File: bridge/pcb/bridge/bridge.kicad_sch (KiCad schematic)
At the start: 14 parts, among them J1 Screw_Terminal_01x06, J2 Screw_Terminal_01x06, J3 Screw_Terminal_01x06, J4 Conn_01x23, SW1 SW_SPST, U2 J104D2C12VDC.20S

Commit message: Completed schematic
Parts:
- added R11: 47k, bridge:THT_RESISTOR_WITH_VALUE, symbol Device:R
- added R12: 100k, bridge:THT_RESISTOR_WITH_VALUE, symbol Device:R
- R6, R7, R8, R9: footprint Resistor_THT:R_Axial_DIN0309_L9.0mm_D3.2mm_P12.70mm_Horizontal -> bridge:THT_RESISTOR_WITH_VALUE
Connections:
- net GND: now also R11.1
- net at R6.1, SW1.1 (A), U2.8: now also R12.2
- new net MAN_AUTO_STATE: R11.2, R12.1
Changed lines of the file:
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@@
     (company "Roman Rice")
   )
+  (junction (at 110.49 144.78) (diameter 0) (color 0 0 0 0)
+  )
   (junction (at 226.06 106.68) (diameter 0) (color 0 0 0 0)
   )
+  (junction (at 110.49 166.37) (diameter 0) (color 0 0 0 0)
+  )
   (junction (at 95.25 144.78) (diameter 0) (color 0 0 0 0)
   )
   (junction (at 111.76 43.18) (diameter 0) (color 0 0 0 0)
+  )
+  (junction (at 128.27 144.78) (diameter 0) (color 0 0 0 0)
   )
   (no_connect (at 228.6 111.76))
@@
     (stroke (width 0) (type default))
   )
+  (wire (pts (xy 128.27 153.67) (xy 128.27 166.37))
+    (stroke (width 0) (type default))
+  )
   (wire (pts (xy 60.96 76.2) (xy 41.91 76.2))
     (stroke (width 0) (type default))
@@
     (stroke (width 0) (type default))
   )
+  (wire (pts (xy 128.27 166.37) (xy 110.49 166.37))
+    (stroke (width 0) (type default))
+  )
   (wire (pts (xy 153.67 81.28) (xy 153.67 83.82))
     (stroke (width 0) (type default))
@@
     (stroke (width 0) (type default))
   )
+  (wire (pts (xy 110.49 167.64) (xy 110.49 166.37))
+    (stroke (width 0) (type default))
+  )
+  (wire (pts (xy 128.27 142.24) (xy 128.27 144.78))
+    (stroke (width 0) (type default))
+  )
+  (wire (pts (xy 110.49 166.37) (xy 110.49 163.83))
+    (stroke (width 0) (type default))
+  )
   (wire (pts (xy 111.76 48.26) (xy 111.76 43.18))
     (stroke (width 0) (type default))
   )
+  (wire (pts (xy 128.27 146.05) (xy 128.27 144.78))
+    (stroke (width 0) (type default))
+  )
   (wire (pts (xy 116.84 50.8) (xy 120.65 50.8))
     (stroke (width 0) (type default))
@@
     (stroke (width 0) (type default))
   )
+  (wire (pts (xy 124.46 144.78) (xy 128.27 144.78))
+    (stroke (width 0) (type default))
+  )
   (wire (pts (xy 210.82 111.76) (xy 210.82 114.3))
     (stroke (width 0) (type default))
   )
+  (wire (pts (xy 110.49 144.78) (xy 116.84 144.78))
+    (stroke (width 0) (type default))
+  )
   (wire (pts (xy 60.96 78.74) (xy 60.96 76.2))
     (stroke (width 0) (type default))
@@
     (fill (type none))
   )
-  (rectangle (start 19.05 118.11) (end 132.08 175.26)
+  (rectangle (start 19.05 118.11) (end 137.16 175.26)
     (stroke (width 0) (type default))
     (fill (type none))
@@
     )
   )
+  (global_label "MAN_AUTO_STATE" (shape input) (at 128.27 142.24 90) (fields_autoplaced)
+    (effects (font (size 1.27 1.27) bold) (justify left))
+    (property "Intersheetrefs" "${INTERSHEET_REFS}" (at 128.27 122.8736 90)
+      (effects (font (size 1.27 1.27)) (justify left) hide)
+    )
+  )
   (global_label "TACH_PULSE" (shape input) (at 228.6 116.84 180) (fields_autoplaced)
     (effects (font (size 1.27 1.27)) (justify right))
@@
       (effects (font (size 1.27 1.27)) (justify left))
     )
-    (property "Footprint" "Resistor_THT:R_Axial_DIN0309_L9.0mm_D3.2mm_P12.70mm_Horizontal" (at 151.892 87.63 90)
+    (property "Footprint" "bridge:THT_RESISTOR_WITH_VALUE" (at 151.892 87.63 90)
       (effects (font (size 1.27 1.27)) hide)
     )
@@
     )
   )
+  (symbol (lib_id "Device:R") (at 120.65 144.78 270) (unit 1)
+    (in_bom yes) (on_board yes) (dnp no) (fields_autoplaced)
+    (property "Reference" "R12" (at 120.65 138.43 90)
+      (effects (font (size 1.27 1.27)))
+    )
+    (property "Value" "100k" (at 120.65 140.97 90)
+      (effects (font (size 1.27 1.27)))
+    )
+    (property "Footprint" "bridge:THT_RESISTOR_WITH_VALUE" (at 120.65 143.002 90)
+      (effects (font (size 1.27 1.27)) hide)
+    )
+    (property "Datasheet" "~" (at 120.65 144.78 0)
+      (effects (font (size 1.27 1.27)) hide)
+    )
+    (pin "1")
+    (pin "2")
+    (instances
+      (project "bridge"
+        (path "/40a0f45e-7290-47b9-8da3-09f7dfbfbbd7"
+          (reference "R12") (unit 1)
+        )
+      )
+    )
+  )
   (symbol (lib_id "power:+BATT") (at 207.01 33.02 0) (mirror y) (unit 1)
     (in_bom yes) (on_board yes) (dnp no) (fields_autoplaced)
@@
       (effects (font (size 1.27 1.27)) (justify left))
     )
-    (property "Footprint" "Resistor_THT:R_Axial_DIN0309_L9.0mm_D3.2mm_P12.70mm_Horizontal" (at 122.682 87.63 90)
+    (property "Footprint" "bridge:THT_RESISTOR_WITH_VALUE" (at 122.682 87.63 90)
       (effects (font (size 1.27 1.27)) hide)
     )
@@
     )
   )
+  (symbol (lib_id "Device:R") (at 128.27 149.86 180) (unit 1)
+    (in_bom yes) (on_board yes) (dnp no) (fields_autoplaced)
+    (property "Reference" "R11" (at 130.81 148.59 0)
+      (effects (font (size 1.27 1.27)) (justify right))
+    )
+    (property "Value" "47k" (at 130.81 151.13 0)
+      (effects (font (size 1.27 1.27)) (justify right))
+    )
+    (property "Footprint" "bridge:THT_RESISTOR_WITH_VALUE" (at 130.048 149.86 90)
+      (effects (font (size 1.27 1.27)) hide)
+    )
+    (property "Datasheet" "~" (at 128.27 149.86 0)
+      (effects (font (size 1.27 1.27)) hide)
+    )
+    (pin "1")
+    (pin "2")
+    (instances
+      (project "bridge"
+        (path "/40a0f45e-7290-47b9-8da3-09f7dfbfbbd7"
+          (reference "R11") (unit 1)
+        )
+      )
+    )
+  )
   (symbol (lib_id "Device:R") (at 139.7 87.63 0) (unit 1)
     (in_bom yes) (on_board yes) (dnp no) (fields_autoplaced)
@@
       (effects (font (size 1.27 1.27)) (justify left))
     )
-    (property "Footprint" "Resistor_THT:R_Axial_DIN0309_L9.0mm_D3.2mm_P12.70mm_Horizontal" (at 137.922 87.63 90)
+    (property "Footprint" "bridge:THT_RESISTOR_WITH_VALUE" (at 137.922 87.63 90)
       (effects (font (size 1.27 1.27)) hide)
     )
@@
     )
   )
-  (symbol (lib_id "power:GND") (at 110.49 163.83 0) (unit 1)
-    (in_bom yes) (on_board yes) (dnp no) (fields_autoplaced)
-    (property "Reference" "#PWR08" (at 110.49 170.18 0)
-      (effects (font (size 1.27 1.27)) hide)
-    )
-    (property "Value" "GND" (at 110.49 168.91 0)
-      (effects (font (size 1.27 1.27)))
-    )
-    (property "Footprint" "" (at 110.49 163.83 0)
-      (effects (font (size 1.27 1.27)) hide)
-    )
-    (property "Datasheet" "" (at 110.49 163.83 0)
+  (symbol (lib_id "power:GND") (at 110.49 167.64 0) (unit 1)
+    (in_bom yes) (on_board yes) (dnp no) (fields_autoplaced)
+    (property "Reference" "#PWR08" (at 110.49 173.99 0)
+      (effects (font (size 1.27 1.27)) hide)
+    )
+    (property "Value" "GND" (at 110.49 172.72 0)
+      (effects (font (size 1.27 1.27)))
+    )
+    (property "Footprint" "" (at 110.49 167.64 0)
+      (effects (font (size 1.27 1.27)) hide)
+    )
+    (property "Datasheet" "" (at 110.49 167.64 0)
       (effects (font (size 1.27 1.27)) hide)
     )
@@
       (effects (font (size 1.27 1.27)) (justify left))
     )
-    (property "Footprint" "Resistor_THT:R_Axial_DIN0309_L9.0mm_D3.2mm_P12.70mm_Horizontal" (at 108.712 149.86 90)
-      (effects (font (size 1.27 1.27)) hide)
-    )
+    (property "Footprint" "bridge:THT_RESISTOR_WITH_VALUE" (at 108.712 149.86 90)
+      (effects (font (size 1.27 1.27)) hide)
+    )

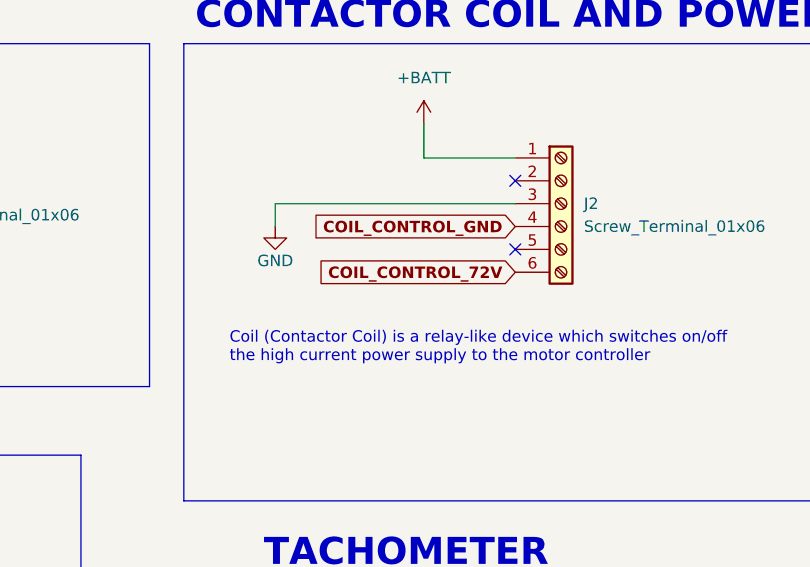
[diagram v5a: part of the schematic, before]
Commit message: Completed routing of PCB
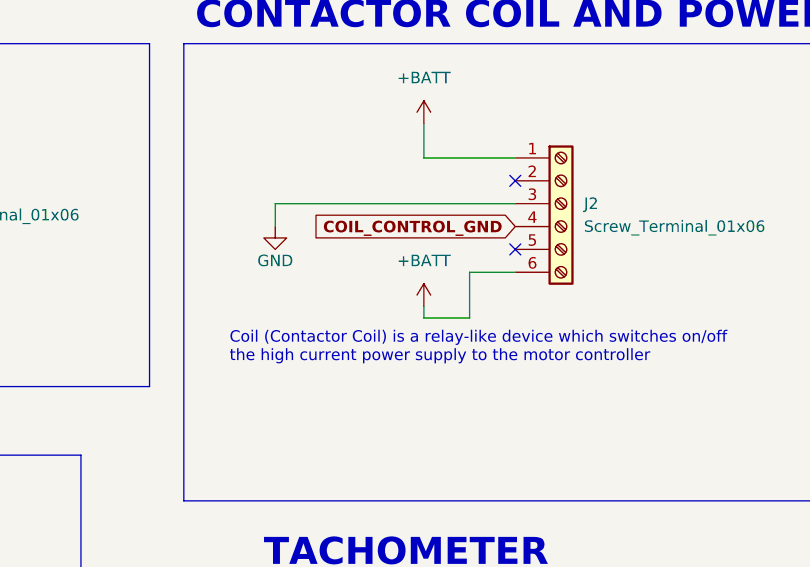
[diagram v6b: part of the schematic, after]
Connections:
- net COIL_CONTROL_72V is gone; now on net +BATT: J2.6 (Pin_6)
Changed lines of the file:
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@@
+    (stroke (width 0) (type default))
+  )
+  (wire (pts (xy 212.09 49.53) (xy 212.09 54.61))
+    (stroke (width 0) (type default))
+  )
+  (wire (pts (xy 212.09 54.61) (xy 207.01 54.61))
     (stroke (width 0) (type default))
   )
@@
     (stroke (width 0) (type default))
   )
+  (wire (pts (xy 217.17 49.53) (xy 212.09 49.53))
+    (stroke (width 0) (type default))
+  )
   (wire (pts (xy 116.84 49.53) (xy 116.84 50.8))
     (stroke (width 0) (type default))
@@
   )
   (wire (pts (xy 128.27 142.24) (xy 128.27 144.78))
+    (stroke (width 0) (type default))
+  )
+  (wire (pts (xy 207.01 54.61) (xy 207.01 53.34))
     (stroke (width 0) (type default))
   )
@@
     (property "Intersheetrefs" "${INTERSHEET_REFS}" (at 55.7126 53.34 0)
       (effects (font (size 1.27 1.27)) (justify left) hide)
-    )
-  )
-  (global_label "COIL_CONTROL_72V" (shape input) (at 217.17 49.53 180) (fields_autoplaced)
-    (effects (font (size 1.27 1.27) bold) (justify right))
-    (property "Intersheetrefs" "${INTERSHEET_REFS}" (at 195.5054 49.53 0)
-      (effects (font (size 1.27 1.27)) (justify right) hide)
     )
   )
@@
         )
       )
+    )
+  )
+  (symbol (lib_id "power:+BATT") (at 207.01 53.34 0) (mirror y) (unit 1)
+    (in_bom yes) (on_board yes) (dnp no) (fields_autoplaced)
+    (property "Reference" "#PWR030" (at 207.01 57.15 0)
+      (effects (font (size 1.27 1.27)) hide)
+    )
+    (property "Value" "+BATT" (at 207.01 48.26 0)
+      (effects (font (size 1.27 1.27)))
+    )
+    (property "Footprint" "" (at 207.01 53.34 0)
+      (effects (font (size 1.27 1.27)) hide)
+    )
+    (property "Datasheet" "" (at 207.01 53.34 0)
+      (effects (font (size 1.27 1.27)) hide)
+    )
+    (pin "1")
+    (instances
+      (project "bridge"
+        (path "/40a0f45e-7290-47b9-8da3-09f7dfbfbbd7"
+          (reference "#PWR030") (unit 1)
+        )
+      )

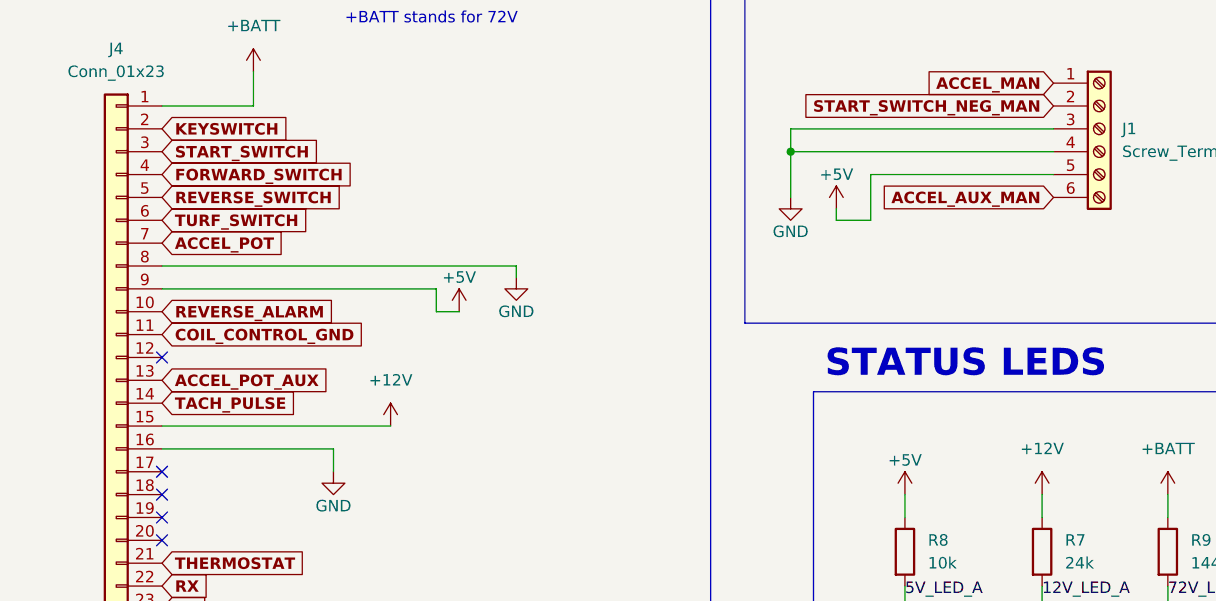
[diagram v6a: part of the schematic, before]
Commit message: Seperated 5V for accel pot and main 5V supply
Added 5V and 12V enable PCB headers
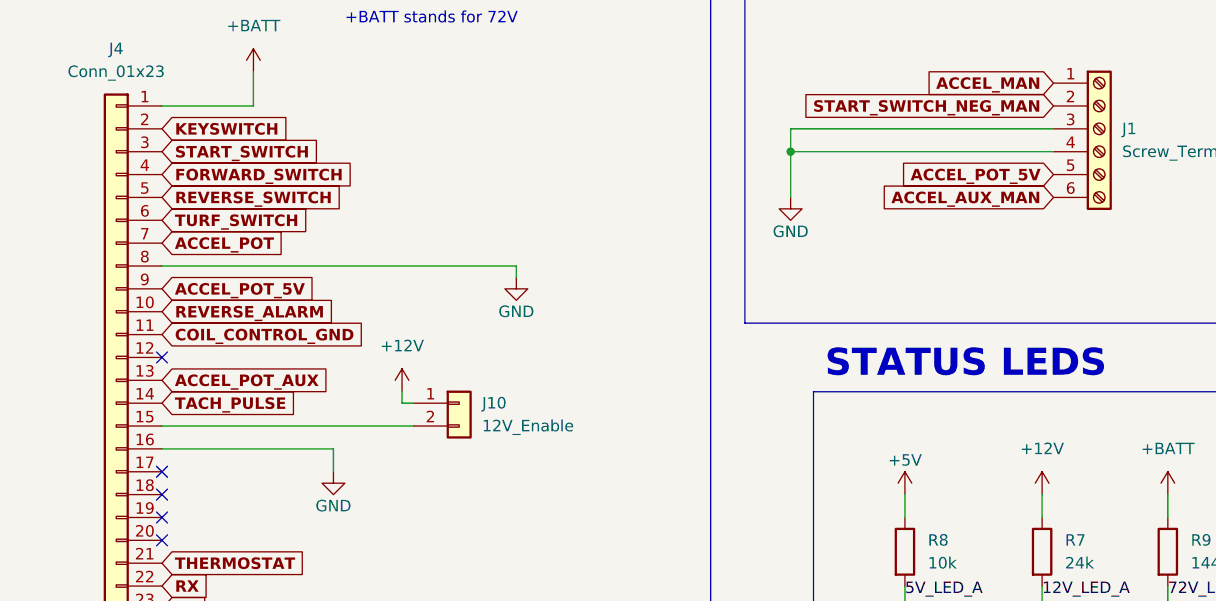
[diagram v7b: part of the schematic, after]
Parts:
- added J10: 12V_Enable, Connector_PinHeader_2.54mm:PinHeader_1x02_P2.54mm_Vertical, symbol Connector_Generic:Conn_01x02
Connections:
- net +12V: now also J10.1 (Pin_1); no longer J4.15 (Pin_15)
- net +5V: no longer J1.5 (Pin_5), J4.9 (Pin_9)
- new net: J10.2 (Pin_2), J4.15 (Pin_15)
- new net ACCEL_POT_5V: J1.5 (Pin_5), J4.9 (Pin_9)
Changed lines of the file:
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@@
   (no_connect (at 41.91 66.04))
   (no_connect (at 41.91 86.36))
-  (wire (pts (xy 74.93 60.96) (xy 72.39 60.96))
-    (stroke (width 0) (type default))
-  )
   (wire (pts (xy 52.07 34.29) (xy 52.07 38.1))
     (stroke (width 0) (type default))
@@
     (stroke (width 0) (type default))
   )
-  (wire (pts (xy 41.91 73.66) (xy 67.31 73.66))
-    (stroke (width 0) (type default))
-  )
-  (wire (pts (xy 72.39 60.96) (xy 72.39 58.42))
+  (wire (pts (xy 41.91 73.66) (xy 69.85 73.66))
     (stroke (width 0) (type default))
   )
@@
     (stroke (width 0) (type default))
   )
-  (wire (pts (xy 120.65 50.8) (xy 120.65 45.72))
-    (stroke (width 0) (type default))
-  )
   (wire (pts (xy 190.5 41.91) (xy 190.5 44.45))
     (stroke (width 0) (type default))
@@
     (stroke (width 0) (type default))
   )
-  (wire (pts (xy 41.91 58.42) (xy 72.39 58.42))
-    (stroke (width 0) (type default))
-  )
   (wire (pts (xy 226.06 106.68) (xy 226.06 109.22))
     (stroke (width 0) (type default))
@@
     (stroke (width 0) (type default))
   )
-  (wire (pts (xy 120.65 45.72) (xy 140.97 45.72))
-    (stroke (width 0) (type default))
-  )
   (wire (pts (xy 228.6 114.3) (xy 213.36 114.3))
     (stroke (width 0) (type default))
   )
+  (wire (pts (xy 68.58 69.85) (xy 68.58 71.12))
+    (stroke (width 0) (type default))
+  )
   (wire (pts (xy 207.01 106.68) (xy 226.06 106.68))
     (stroke (width 0) (type default))
@@
     (stroke (width 0) (type default))
   )
+  (wire (pts (xy 68.58 71.12) (xy 69.85 71.12))
+    (stroke (width 0) (type default))
+  )
   (wire (pts (xy 128.27 166.37) (xy 110.49 166.37))
     (stroke (width 0) (type default))
@@
     (stroke (width 0) (type default))
   )
-  (wire (pts (xy 116.84 49.53) (xy 116.84 50.8))
-    (stroke (width 0) (type default))
-  )
   (wire (pts (xy 110.49 167.64) (xy 110.49 166.37))
     (stroke (width 0) (type default))
@@
   )
   (wire (pts (xy 128.27 146.05) (xy 128.27 144.78))
-    (stroke (width 0) (type default))
-  )
-  (wire (pts (xy 116.84 50.8) (xy 120.65 50.8))
     (stroke (width 0) (type default))
   )
@@
     )
   )
+  (global_label "ACCEL_POT_5V" (shape input) (at 140.97 45.72 180) (fields_autoplaced)
+    (effects (font (size 1.27 1.27) bold) (justify right))
+    (property "Intersheetrefs" "${INTERSHEET_REFS}" (at 123.9017 45.72 0)
+      (effects (font (size 1.27 1.27)) (justify right) hide)
+    )
+  )
   (global_label "ACCEL_AUTO" (shape input) (at 90.17 154.94 0) (fields_autoplaced)
     (effects (font (size 1.27 1.27) (thickness 0.254) bold) (justify left))
@@
     (property "Intersheetrefs" "${INTERSHEET_REFS}" (at 213.8825 104.14 0)
       (effects (font (size 1.27 1.27)) (justify right) hide)
+    )
+  )
+  (global_label "ACCEL_POT_5V" (shape input) (at 41.91 58.42 0) (fields_autoplaced)
+    (effects (font (size 1.27 1.27) bold) (justify left))
+    (property "Intersheetrefs" "${INTERSHEET_REFS}" (at 58.9783 58.42 0)
+      (effects (font (size 1.27 1.27)) (justify left) hide)
     )
   )
@@
     )
   )
-  (symbol (lib_id "power:+5V") (at 74.93 60.96 0) (unit 1)
-    (in_bom yes) (on_board yes) (dnp no)
-    (property "Reference" "#PWR03" (at 74.93 64.77 0)
-      (effects (font (size 1.27 1.27)) hide)
-    )
-    (property "Value" "+5V" (at 74.93 57.15 0)
-      (effects (font (size 1.27 1.27)))
-    )
-    (property "Footprint" "" (at 74.93 60.96 0)
-      (effects (font (size 1.27 1.27)) hide)
-    )
-    (property "Datasheet" "" (at 74.93 60.96 0)
-      (effects (font (size 1.27 1.27)) hide)
-    )
-    (pin "1")
-    (instances
-      (project "bridge"
-        (path "/40a0f45e-7290-47b9-8da3-09f7dfbfbbd7"
-          (reference "#PWR03") (unit 1)
-        )
-      )
-    )
-  )
   (symbol (lib_id "power:GND") (at 124.46 101.6 0) (unit 1)
     (in_bom yes) (on_board yes) (dnp no) (fields_autoplaced)
@@
     )
   )
+  (symbol (lib_id "Connector_Generic:Conn_01x02") (at 74.93 71.12 0) (unit 1)
+    (in_bom yes) (on_board yes) (dnp no) (fields_autoplaced)
+    (property "Reference" "J10" (at 77.47 71.12 0)
+      (effects (font (size 1.27 1.27)) (justify left))
+    )
+    (property "Value" "12V_Enable" (at 77.47 73.66 0)
+      (effects (font (size 1.27 1.27)) (justify left))
+    )
+    (property "Footprint" "Connector_PinHeader_2.54mm:PinHeader_1x02_P2.54mm_Vertical" (at 74.93 71.12 0)
+      (effects (font (size 1.27 1.27)) hide)
+    )
+    (property "Datasheet" "~" (at 74.93 71.12 0)
+      (effects (font (size 1.27 1.27)) hide)
+    )
+    (pin "1")
+    (pin "2")
+    (instances
+      (project "bridge"
+        (path "/40a0f45e-7290-47b9-8da3-09f7dfbfbbd7"
+          (reference "J10") (unit 1)
+        )
+      )
+    )
+  )
   (symbol (lib_id "Connector:Screw_Terminal_01x06") (at 233.68 109.22 0) (unit 1)
     (in_bom yes) (on_board yes) (dnp no) (fields_autoplaced)
@@
     )
   )
-  (symbol (lib_id "power:+5V") (at 116.84 49.53 0) (unit 1)
-    (in_bom yes) (on_board yes) (dnp no)
-    (property "Reference" "#PWR010" (at 116.84 53.34 0)
-      (effects (font (size 1.27 1.27)) hide)
-    )
-    (property "Value" "+5V" (at 116.84 45.72 0)
-      (effects (font (size 1.27 1.27)))
-    )
-    (property "Footprint" "" (at 116.84 49.53 0)
-      (effects (font (size 1.27 1.27)) hide)
-    )
-    (property "Datasheet" "" (at 116.84 49.53 0)
-      (effects (font (size 1.27 1.27)) hide)
-    )
-    (pin "1")
-    (instances
-      (project "bridge"
-        (path "/40a0f45e-7290-47b9-8da3-09f7dfbfbbd7"
-          (reference "#PWR010") (unit 1)
-        )
-      )
-    )
-  )
   (symbol (lib_id "power:GND") (at 110.49 167.64 0) (unit 1)
     (in_bom yes) (on_board yes) (dnp no) (fields_autoplaced)
@@
         (path "/40a0f45e-7290-47b9-8da3-09f7dfbfbbd7"
           (reference "#PWR08") (unit 1)
-        )
-      )
-    )
-  )
-  (symbol (lib_id "power:+12V") (at 67.31 73.66 0) (unit 1)
-    (in_bom yes) (on_board yes) (dnp no) (fields_autoplaced)
-    (property "Reference" "#PWR05" (at 67.31 77.47 0)
-      (effects (font (size 1.27 1.27)) hide)
-    )
-    (property "Value" "+12V" (at 67.31 68.58 0)
-      (effects (font (size 1.27 1.27)))
-    )
-    (property "Footprint" "" (at 67.31 73.66 0)
-      (effects (font (size 1.27 1.27)) hide)
-    )
-    (property "Datasheet" "" (at 67.31 73.66 0)
-      (effects (font (size 1.27 1.27)) hide)
-    )
-    (pin "1")
-    (instances
-      (project "bridge"
-        (path "/40a0f45e-7290-47b9-8da3-09f7dfbfbbd7"
-          (reference "#PWR05") (unit 1)
         )
       )
@@
         )
       )
+    )
+  )
+  (symbol (lib_id "power:+12V") (at 68.58 69.85 0) (unit 1)
+    (in_bom yes) (on_board yes) (dnp no) (fields_autoplaced)
+    (property "Reference" "#PWR03" (at 68.58 73.66 0)
+      (effects (font (size 1.27 1.27)) hide)
+    )
+    (property "Value" "+12V" (at 68.58 64.77 0)
+      (effects (font (size 1.27 1.27)))
+    )
+    (property "Footprint" "" (at 68.58 69.85 0)
+      (effects (font (size 1.27 1.27)) hide)
+    )
+    (property "Datasheet" "" (at 68.58 69.85 0)
+      (effects (font (size 1.27 1.27)) hide)
+    )
+    (pin "1")
+    (instances
+      (project "bridge"
+        (path "/40a0f45e-7290-47b9-8da3-09f7dfbfbbd7"
+          (reference "#PWR03") (unit 1)
+        )
+      )
